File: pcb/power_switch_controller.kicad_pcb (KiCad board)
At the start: 2 copper layers, 118.1 x 54.6 mm, 38 parts, among them P1 PWR_JACK_2.5x5.5, P2 HEADER_01X03, P3 BNC_DOUBLE_RA, P4 HEADER_02X08, P5 HEADER_02X08, SW1 SPST_SERIES_M, U1 MAX6817, U2 TLE723X, U3 TLE723X

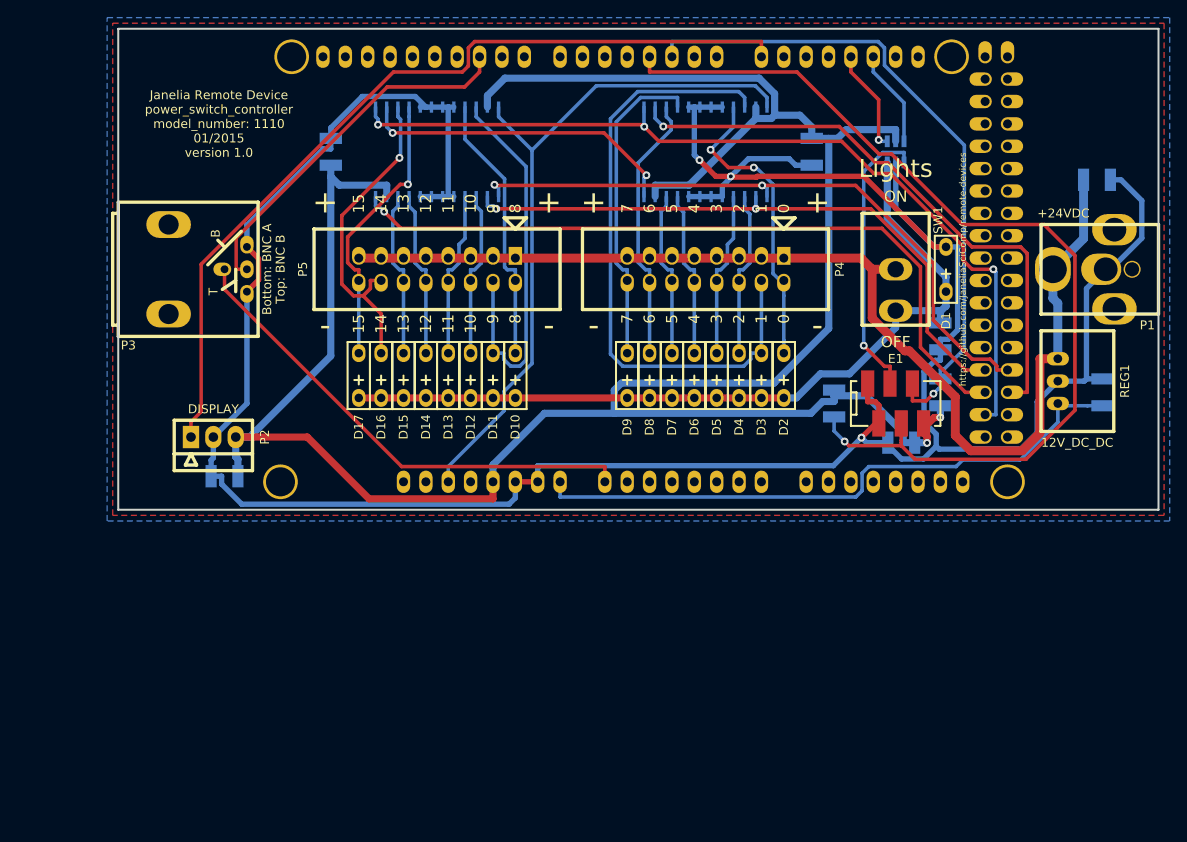
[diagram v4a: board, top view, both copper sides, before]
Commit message: Progress towards 32 power switches.
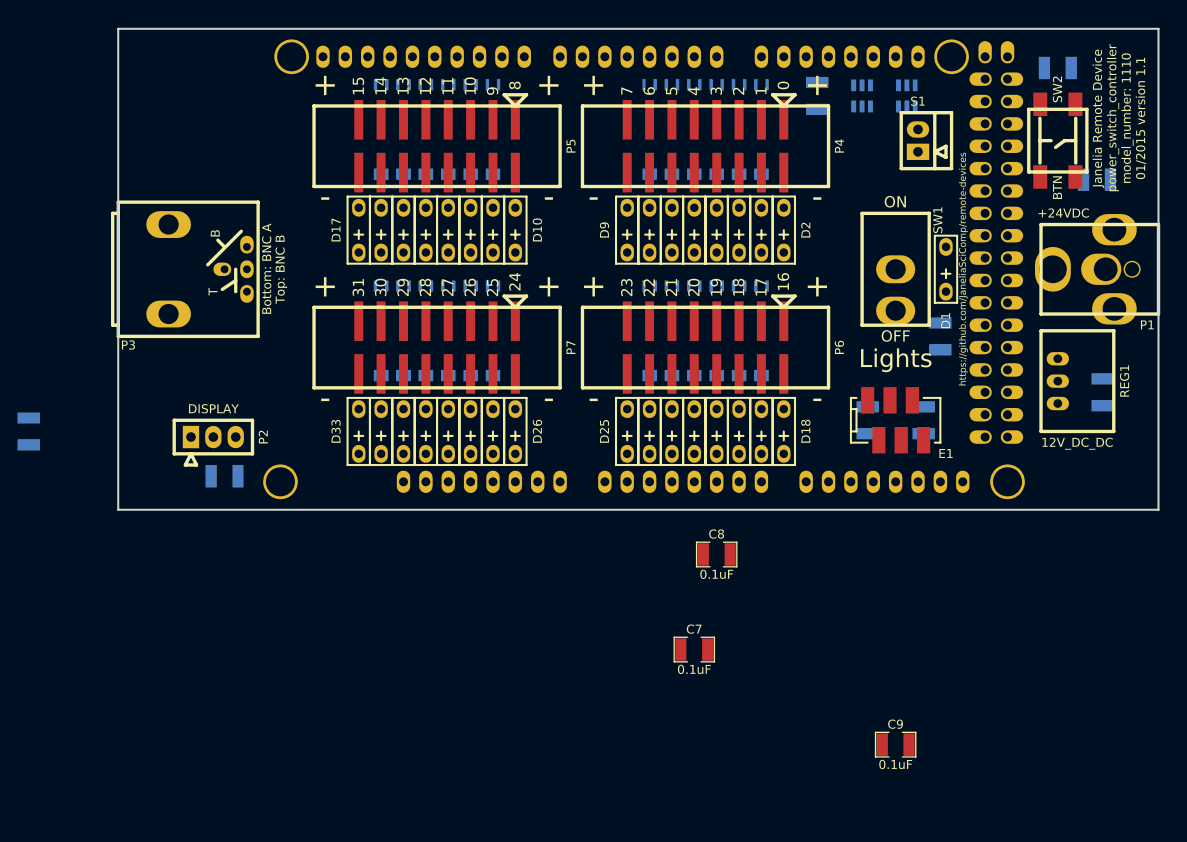
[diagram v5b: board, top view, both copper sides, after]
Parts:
- added C7: 0.1uF, power_switch_controller:SM1210, F.Cu at (158.8, 146.1)
- added C8: 0.1uF, power_switch_controller:SM1210, F.Cu at (161.3, 135.3)
- added C9: 0.1uF, power_switch_controller:SM1210, F.Cu at (181.6, 156.8)
- added D18: LED_24V, power_switch_controller:LED_555-3XXX, F.Cu at (168.9, 121.3)
- added D19: LED_24V, power_switch_controller:LED_555-3XXX, F.Cu at (166.4, 121.3)
- added D20: LED_24V, power_switch_controller:LED_555-3XXX, F.Cu at (163.8, 121.3)
- added D21: LED_24V, power_switch_controller:LED_555-3XXX, F.Cu at (161.3, 121.3)
- added D22: LED_24V, power_switch_controller:LED_555-3XXX, F.Cu at (158.8, 121.3)
- added D23: LED_24V, power_switch_controller:LED_555-3XXX, F.Cu at (156.2, 121.3)
- added D24: LED_24V, power_switch_controller:LED_555-3XXX, F.Cu at (153.7, 121.3)
- added D25: LED_24V, power_switch_controller:LED_555-3XXX, F.Cu at (151.1, 121.3)
- added D26: LED_24V, power_switch_controller:LED_555-3XXX, F.Cu at (138.4, 121.3)
- added D27: LED_24V, power_switch_controller:LED_555-3XXX, F.Cu at (135.9, 121.3)
- added D28: LED_24V, power_switch_controller:LED_555-3XXX, F.Cu at (133.3, 121.3)
- added D29: LED_24V, power_switch_controller:LED_555-3XXX, F.Cu at (130.8, 121.3)
- added D30: LED_24V, power_switch_controller:LED_555-3XXX, F.Cu at (128.3, 121.3)
- added D31: LED_24V, power_switch_controller:LED_555-3XXX, F.Cu at (125.7, 121.3)
- added D32: LED_24V, power_switch_controller:LED_555-3XXX, F.Cu at (123.2, 121.3)
- added D33: LED_24V, power_switch_controller:LED_555-3XXX, F.Cu at (120.7, 121.3)
- added P6: HEADER_02X08_SMD, power_switch_controller:HEADER_02x08_SMD, F.Cu at (160.0, 111.8)
- added P7: HEADER_02X08_SMD, power_switch_controller:HEADER_02x08_SMD, F.Cu at (129.5, 111.8)
- added S1: HEADER_01X02_SHR, power_switch_controller:Header_Shrouded_2_Pin, F.Cu at (184.2, 88.3)
- added SW2: KT_SWITCH, power_switch_controller:KT_SWITCH, F.Cu at (200.0, 88.3)
- added U4: TLE723X, power_switch_controller:TLE723X, B.Cu at (129.5, 87.0)
- added U5: TLE723X, power_switch_controller:TLE723X, B.Cu at (160.0, 109.9)
- added U6: TLE723X, power_switch_controller:TLE723X, B.Cu at (129.5, 109.9)
- P2: footprint power_switch_controller:Header_Shrouded_3_Pin -> footprints:Header_3_Pin
- P4, P5: value HEADER_02X08 -> HEADER_02X08_SMD; footprint power_switch_controller:HEADER_02x08 -> power_switch_controller:HEADER_02x08_SMD
- U2: value TLE723X -> MAX6817; footprint power_switch_controller:TLE723X -> power_switch_controller:MAX6817
- moved C6 46.7 mm to (83.2, 121.3)
- moved C4 40.5 mm to (172.7, 83.2), turned to 270 degrees
- moved U3 30.6 mm to (160.0, 87.0)
- moved C5 29.5 mm to (200.0, 80.0), turned to 0 degrees
- moved U2 23.7 mm to (182.9, 83.2), turned to 90 degrees
- moved D10 16.5 mm to (138.4, 98.4)
- moved D11 16.5 mm to (135.9, 98.4)
- moved D12 16.5 mm to (133.3, 98.4)
- moved D13 16.5 mm to (130.8, 98.4)
- moved D14 16.5 mm to (128.3, 98.4)
- moved D15 16.5 mm to (125.7, 98.4)
- moved D16 16.5 mm to (123.2, 98.4)
- moved D17 16.5 mm to (120.7, 98.4)
- moved D2 16.5 mm to (168.9, 98.4)
- moved D3 16.5 mm to (166.4, 98.4)
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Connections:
- ARDUINO1 pad 20: (no net) -> /D_IN
- ARDUINO1 pad 21: (no net) -> /D_BTN
- ARDUINO1 pad 5V_4: (no net) -> +5VD
- C4 pad 1: +5V -> +5VD
- C5 pad 1: +5V -> +5VD
- R3 pad 1: GND -> /LED_PWR
- R3 pad 2: /LED_PWR -> GND
- U1 pad 5: +5V -> +5VD
- U2 pad 1: /CS -> /BTN
- U2 pad 2: /IN -> GND
- U2 pad 3: /OUT2 -> /IN
- U2 pad 4: /OUT3 -> /D_IN
- U2 pad 5: GND -> +5VD
- U2 pad 6: GND -> /D_BTN
- U3 pad 10: /OUT13 -> /OUT5
- U3 pad 12: /MISO -> /SI1
- U3 pad 14: /SI1 -> /MOSI
- U3 pad 15: /OUT14 -> /OUT6
- U3 pad 16: /OUT15 -> /OUT7
- U3 pad 21: /OUT8 -> /OUT0
- U3 pad 22: /OUT9 -> /OUT1
- U3 pad 3: /OUT10 -> /OUT2
- U3 pad 4: /OUT11 -> /OUT3
- U3 pad 9: /OUT12 -> /OUT4
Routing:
- net GND: track 327.8 -> 0.00 mm, vias 3 -> 0
- net +5V: track 273.5 -> 0.00 mm, vias 2 -> 0
- net VAA: track 128.2 -> 0.00 mm
- net /ENC_B: track 111.3 -> 0.00 mm, vias 1 -> 0
- net /SCK: track 99.8 -> 0.00 mm, vias 3 -> 0
- net /TX3: track 97.1 -> 0.00 mm
- net /LED_PWR: track 92.6 -> 0.00 mm
- net /MISO: track 84.4 -> 0.00 mm, vias 1 -> 0
- net /RST: track 79.4 -> 0.00 mm
- net /ENC_A: track 75.7 -> 0.00 mm, vias 1 -> 0
- net /CS: track 74.4 -> 0.00 mm, vias 2 -> 0
- net /OUT1: track 71.6 -> 0.00 mm
- net /IN: track 71.1 -> 0.00 mm, vias 2 -> 0
- net /V_IN: track 70.1 -> 0.00 mm
- net /MOSI: track 67.9 -> 0.00 mm, vias 1 -> 0
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- removed copper zone on B.Cu, net GND
- removed copper zone on F.Cu, net VAA
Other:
- board text added: "16"
- board text added: "17"
- board text added: "18"
- board text added: "19"
- board text added: "20"
- board text added: "21"
- board text added: "22"
- board text added: "23"
- board text added: "24"
- board text added: "25"
- board text added: "26"
- board text added: "27"
- board text added: "28"
- board text added: "29"
- board text added: "30"
- board text added: "31"
- board text added: "Janelia Remote Device power_switch_controller model_number: 1110 01/2015 version 1.1"
- board text removed: "Janelia Remote Device power_switch_controller model_number: 1110 01/2015 version 1.0"

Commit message: Finished pcb v1.1.
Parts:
- C7, C8, C9: moved to B.Cu
- moved C6 95.2 mm to (172.7, 88.9)
- moved C9 61.7 mm to (141.6, 109.9), turned to 270 degrees
- moved C7 61.5 mm to (141.6, 87.0), turned to 270 degrees
- moved C8 27.6 mm to (172.1, 109.9), turned to 270 degrees
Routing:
- net GND: track 0.00 -> 455.1 mm, vias 0 -> 6
- net +5V: track 0.00 -> 271.9 mm, vias 0 -> 6
- net /CS: track 0.00 -> 239.1 mm, vias 0 -> 4
- net VAA: track 0.00 -> 215.1 mm, vias 0 -> 1
- net /IN: track 0.00 -> 184.1 mm, vias 0 -> 4
- net /LED_PWR: track 0.00 -> 177.3 mm, vias 0 -> 2
- net /SCK: track 0.00 -> 156.1 mm, vias 0 -> 3
- net /RST: track 0.00 -> 135.0 mm, vias 0 -> 5
- net /TX3: track 0.00 -> 97.9 mm
- net /MOSI: track 0.00 -> 93.3 mm
- net /MISO: track 0.00 -> 75.5 mm, vias 0 -> 2
- net /ENC_B: track 0.00 -> 73.5 mm, vias 0 -> 1
- net /V_IN: track 0.00 -> 69.4 mm
- net /ENC_A: track 0.00 -> 64.7 mm, vias 0 -> 1
- net /BNC_A: track 0.00 -> 55.4 mm, vias 0 -> 1
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- added copper zone on B.Cu, net GND
- added copper zone on F.Cu, net VAA

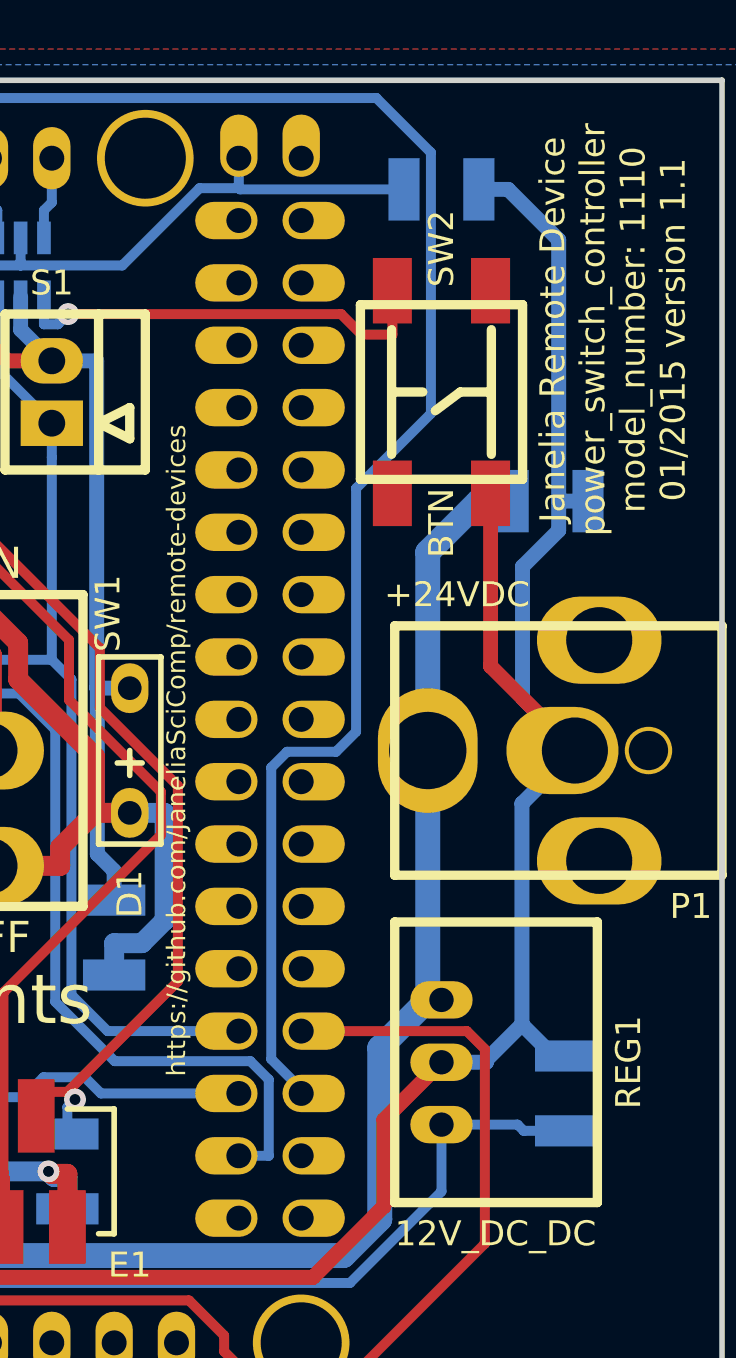
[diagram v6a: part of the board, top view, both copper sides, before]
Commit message: remote -> modular.
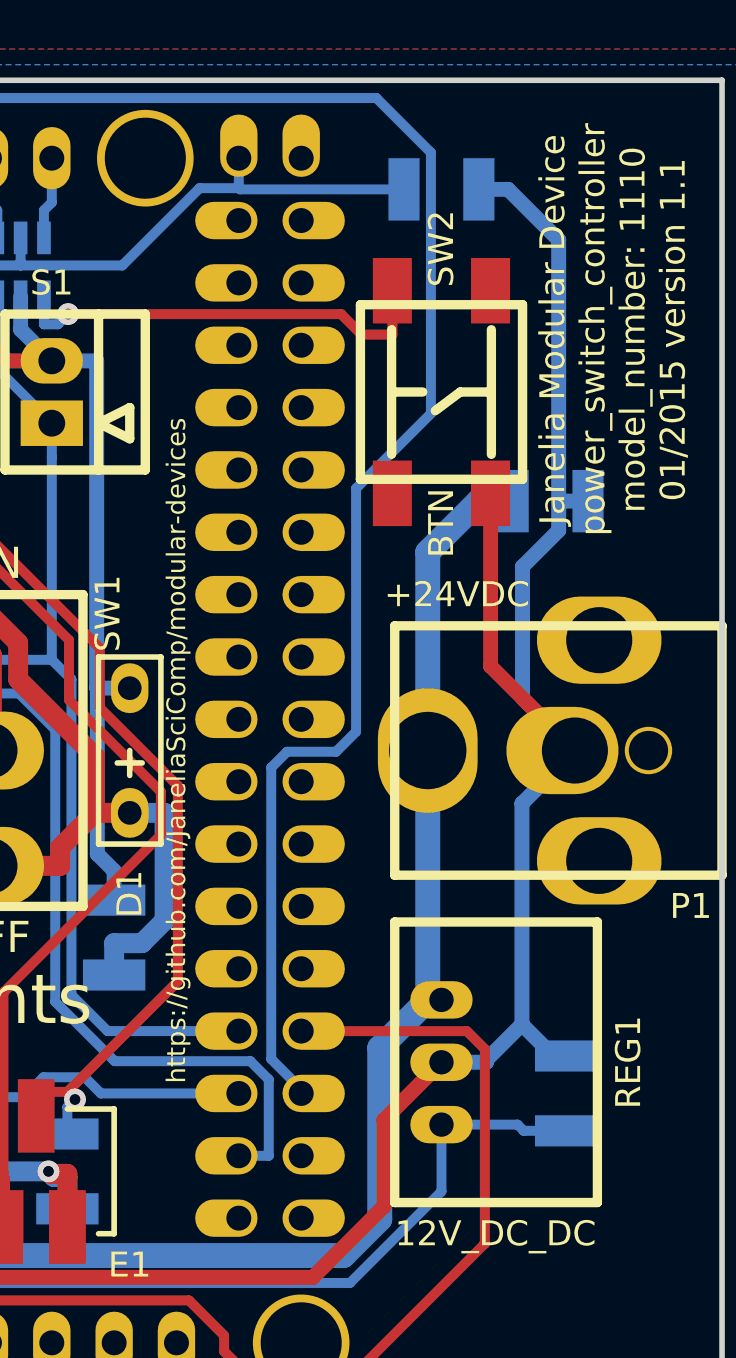
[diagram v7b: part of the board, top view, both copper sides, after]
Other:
- board text added: "Janelia Modular Device power_switch_controller model_number: 1110 01/2015 version 1.1"
- board text added: "https://github.com/JaneliaSciComp/modular-devices"
- board text removed: "Janelia Remote Device power_switch_controller model_number: 1110 01/2015 version 1.1"
- board text removed: "https://github.com/JaneliaSciComp/remote-devices"
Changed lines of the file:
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@@
     (effects (font (size 1.016 1.016) (thickness 0.254)))
   )
-  (gr_text https://github.com/JaneliaSciComp/remote-devices (at 189.23 102.87 90) (layer F.SilkS)
+  (gr_text https://github.com/JaneliaSciComp/modular-devices (at 189.23 102.87 90) (layer F.SilkS)
     (effects (font (size 0.762 0.762) (thickness 0.1905)))
   )
-  (gr_text "Janelia Remote Device\npower_switch_controller\nmodel_number: 1110\n01/2015 version 1.1" (at 207.01 85.725 90) (layer F.SilkS)
+  (gr_text "Janelia Modular Device\npower_switch_controller\nmodel_number: 1110\n01/2015 version 1.1" (at 207.01 85.725 90) (layer F.SilkS)
     (effects (font (size 1.016 1.016) (thickness 0.254)))
   )

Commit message: pcb v1.2.
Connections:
- net /D_IN renamed /D_SWITCH
- ARDUINO1 pad 0: (no net) -> Net-(ARDUINO1-Pad0)
- ARDUINO1 pad 1: (no net) -> Net-(ARDUINO1-Pad1)
- ARDUINO1 pad 10: /BNC_B -> Net-(ARDUINO1-Pad10)
- ARDUINO1 pad 11: (no net) -> Net-(ARDUINO1-Pad11)
- ARDUINO1 pad 12: (no net) -> Net-(ARDUINO1-Pad12)
- ARDUINO1 pad 13: (no net) -> Net-(ARDUINO1-Pad13)
- ARDUINO1 pad 15: (no net) -> Net-(ARDUINO1-Pad15)
- ARDUINO1 pad 16: (no net) -> Net-(ARDUINO1-Pad16)
- ARDUINO1 pad 17: (no net) -> /D_LED_PWR
- ARDUINO1 pad 18: /D_LED_PWR -> /ENC_A
- ARDUINO1 pad 2: /ENC_A -> /ENC_B
- ARDUINO1 pad 20B: (no net) -> Net-(ARDUINO1-Pad20B)
- ARDUINO1 pad 21B: (no net) -> Net-(ARDUINO1-Pad21B)
- ARDUINO1 pad 22: (no net) -> Net-(ARDUINO1-Pad22)
- ARDUINO1 pad 23: (no net) -> Net-(ARDUINO1-Pad23)
- ARDUINO1 pad 24: (no net) -> Net-(ARDUINO1-Pad24)
- ARDUINO1 pad 25: (no net) -> Net-(ARDUINO1-Pad25)
- ARDUINO1 pad 26: (no net) -> Net-(ARDUINO1-Pad26)
- ARDUINO1 pad 27: (no net) -> Net-(ARDUINO1-Pad27)
- ARDUINO1 pad 28: (no net) -> Net-(ARDUINO1-Pad28)
- ARDUINO1 pad 29: (no net) -> Net-(ARDUINO1-Pad29)
- ARDUINO1 pad 3: /ENC_B -> /BNC_B
- ARDUINO1 pad 30: (no net) -> Net-(ARDUINO1-Pad30)
- ARDUINO1 pad 31: (no net) -> Net-(ARDUINO1-Pad31)
- ARDUINO1 pad 32: (no net) -> Net-(ARDUINO1-Pad32)
- ARDUINO1 pad 33: (no net) -> Net-(ARDUINO1-Pad33)
- ARDUINO1 pad 34: (no net) -> Net-(ARDUINO1-Pad34)
- ARDUINO1 pad 35: (no net) -> Net-(ARDUINO1-Pad35)
- ARDUINO1 pad 36: (no net) -> Net-(ARDUINO1-Pad36)
- ARDUINO1 pad 37: (no net) -> Net-(ARDUINO1-Pad37)
- ARDUINO1 pad 38: (no net) -> Net-(ARDUINO1-Pad38)
- ARDUINO1 pad 39: (no net) -> Net-(ARDUINO1-Pad39)
- ARDUINO1 pad 3V3: (no net) -> Net-(ARDUINO1-Pad3V3)
- ARDUINO1 pad 4: (no net) -> Net-(ARDUINO1-Pad4)
- ARDUINO1 pad 40: (no net) -> Net-(ARDUINO1-Pad40)
- ARDUINO1 pad 41: (no net) -> Net-(ARDUINO1-Pad41)
- ARDUINO1 pad 42: (no net) -> Net-(ARDUINO1-Pad42)
- ARDUINO1 pad 43: (no net) -> Net-(ARDUINO1-Pad43)
- ARDUINO1 pad 44: (no net) -> Net-(ARDUINO1-Pad44)
- ARDUINO1 pad 45: (no net) -> Net-(ARDUINO1-Pad45)
- ARDUINO1 pad 46: (no net) -> Net-(ARDUINO1-Pad46)
- ARDUINO1 pad 47: (no net) -> Net-(ARDUINO1-Pad47)
- ARDUINO1 pad 5: (no net) -> Net-(ARDUINO1-Pad5)
- ARDUINO1 pad 53: (no net) -> Net-(ARDUINO1-Pad53)
- ARDUINO1 pad 5V_5: (no net) -> Net-(ARDUINO1-Pad5V_5)
- ARDUINO1 pad 6: (no net) -> Net-(ARDUINO1-Pad6)
- ARDUINO1 pad 7: (no net) -> Net-(ARDUINO1-Pad7)
- ARDUINO1 pad 8: (no net) -> Net-(ARDUINO1-Pad8)
- ARDUINO1 pad 9: (no net) -> Net-(ARDUINO1-Pad9)
- ARDUINO1 pad A1: (no net) -> Net-(ARDUINO1-PadA1)
- ARDUINO1 pad A10: (no net) -> Net-(ARDUINO1-PadA10)
- ARDUINO1 pad A11: (no net) -> Net-(ARDUINO1-PadA11)
- ARDUINO1 pad A12: (no net) -> Net-(ARDUINO1-PadA12)
- ARDUINO1 pad A13: (no net) -> Net-(ARDUINO1-PadA13)
- ARDUINO1 pad A14: (no net) -> Net-(ARDUINO1-PadA14)
- ARDUINO1 pad A15: (no net) -> Net-(ARDUINO1-PadA15)
- ARDUINO1 pad A2: (no net) -> Net-(ARDUINO1-PadA2)
- ARDUINO1 pad A3: (no net) -> Net-(ARDUINO1-PadA3)
- ARDUINO1 pad A4: (no net) -> Net-(ARDUINO1-PadA4)
- ARDUINO1 pad A5: (no net) -> Net-(ARDUINO1-PadA5)
- ARDUINO1 pad A6: (no net) -> Net-(ARDUINO1-PadA6)
- ARDUINO1 pad A7: (no net) -> Net-(ARDUINO1-PadA7)
- ARDUINO1 pad A8: (no net) -> Net-(ARDUINO1-PadA8)
- ARDUINO1 pad A9: (no net) -> Net-(ARDUINO1-PadA9)
- ARDUINO1 pad AREF: (no net) -> Net-(ARDUINO1-PadAREF)
- ARDUINO1 pad GND3: (no net) -> Net-(ARDUINO1-PadGND3)
- ARDUINO1 pad GND4: (no net) -> Net-(ARDUINO1-PadGND4)
- ARDUINO1 pad GND5: (no net) -> Net-(ARDUINO1-PadGND5)
- ARDUINO1 pad IREF: (no net) -> Net-(ARDUINO1-PadIREF)
- ARDUINO1 pad NC: (no net) -> Net-(ARDUINO1-PadNC)
- S1 pad 1: /IN -> /SWITCH
- U2 pad 3: /IN -> /SWITCH
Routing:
- net /CS: track 239.1 -> 171.1 mm, vias 4 -> 3
- net /IN: track 184.1 -> 141.0 mm, vias 4 -> 5
- net /ENC_B: track 73.5 -> 104.7 mm
- net /RST: track 135.0 -> 164.0 mm, vias 5 -> 3
- net /MOSI: track 93.3 -> 65.0 mm, vias 0 -> 1
- net /BNC_A: track 55.4 -> 76.7 mm, vias 1 -> 0
- net /OUT16: track 22.6 -> 43.6 mm, vias 1 -> 0
- net /BNC_B: track 43.1 -> 62.5 mm, vias 1 -> 0
- net +5VD: track 31.8 -> 47.4 mm
- net VAA: track 215.1 -> 203.1 mm
- net +5V: track 271.9 -> 260.3 mm, vias 6 -> 1
- net /SI1: track 36.2 -> 47.6 mm
- net /OUT22: track 15.9 -> 26.1 mm, vias 1 -> 0
- net /OUT14: track 26.2 -> 16.5 mm, vias 0 -> 1
- net /OUT9: track 26.2 -> 35.8 mm, vias 0 -> 1
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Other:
- net class GND: trace_width 0.6096 -> 0.508
- net class LEDPOWER added: clearance 0.254, trace_width 0.508, via_dia 0.889, via_drill 0.635
- board text added: "Janelia Modular Device power_switch_controller model_number: 1110 02/2015 version 1.2"
- board text added: "SWITCH"
- board text removed: "Janelia Modular Device power_switch_controller model_number: 1110 01/2015 version 1.1"
